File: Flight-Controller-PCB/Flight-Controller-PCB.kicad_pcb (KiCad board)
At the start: 2 copper layers, 50 x 50 mm, 77 parts, among them J1 ESC_1, J2 Receiver, J3 ESC_2, J4 ICSP, J5 ESC_3, J6 Aux, J7 ESC_4, J8 Power_In, J9 USB_B_Micro, Q1 BSS138, Q2 BSS138, Q3 PMV48XP,215, Q4 PMV48XP,215, SW1 Push-Switch, U1 MCP6001U, U2 ICM-20689, U3 ATmega32U4-AU, U4 LM1117-5.0, U5 LP2985-3.3, Y1 16MHz, CL 7pF

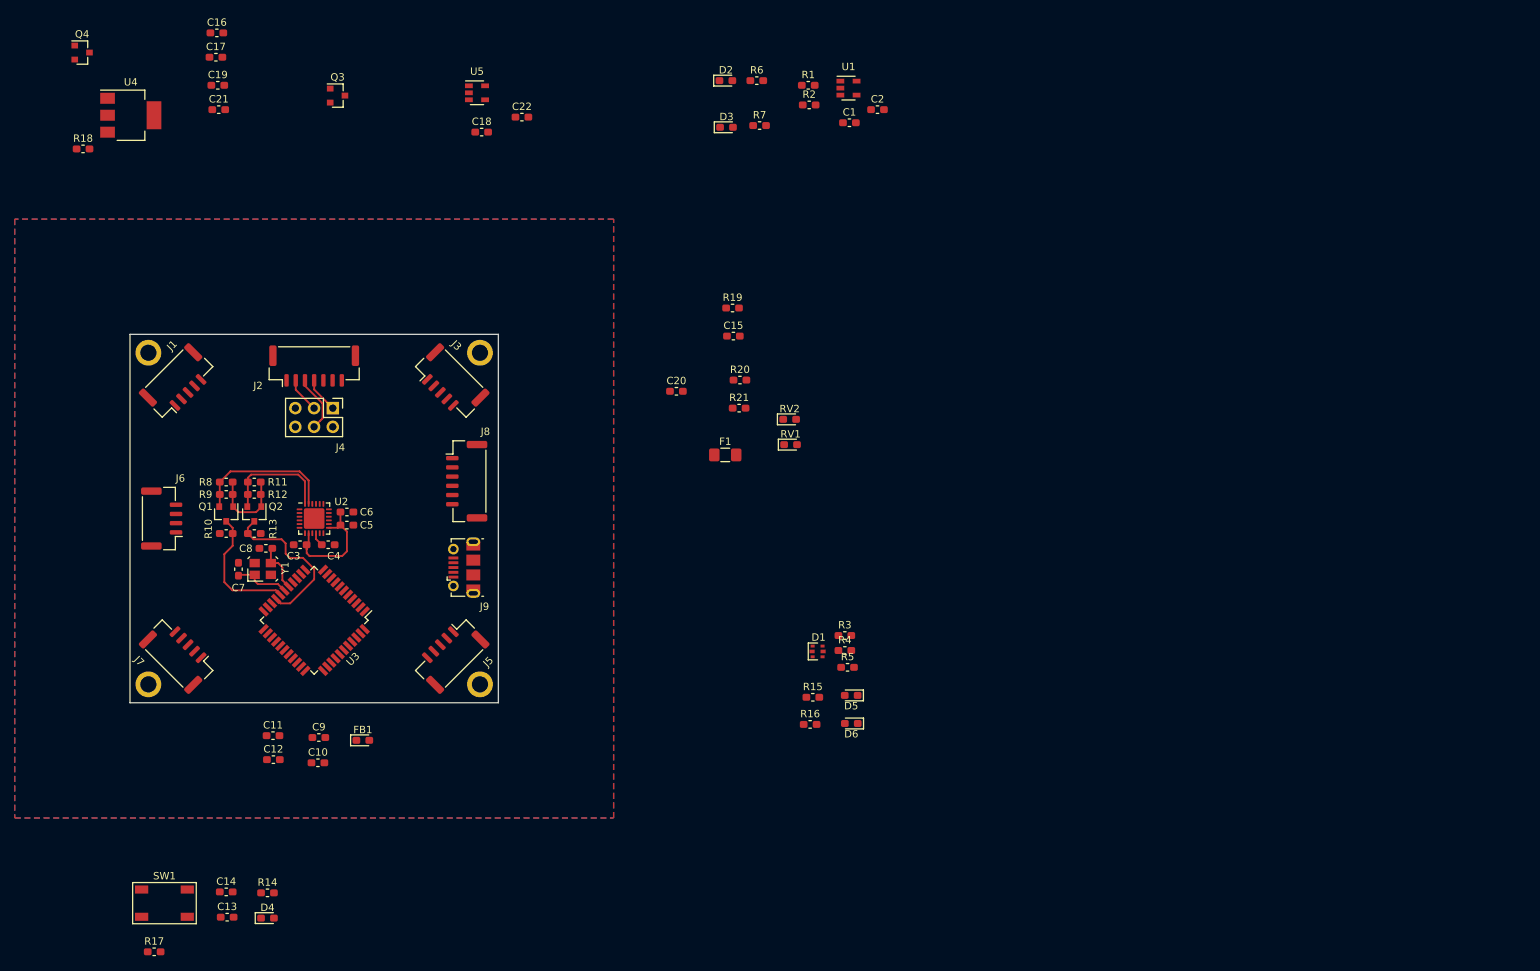
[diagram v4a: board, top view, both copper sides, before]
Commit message: Power regulators routed
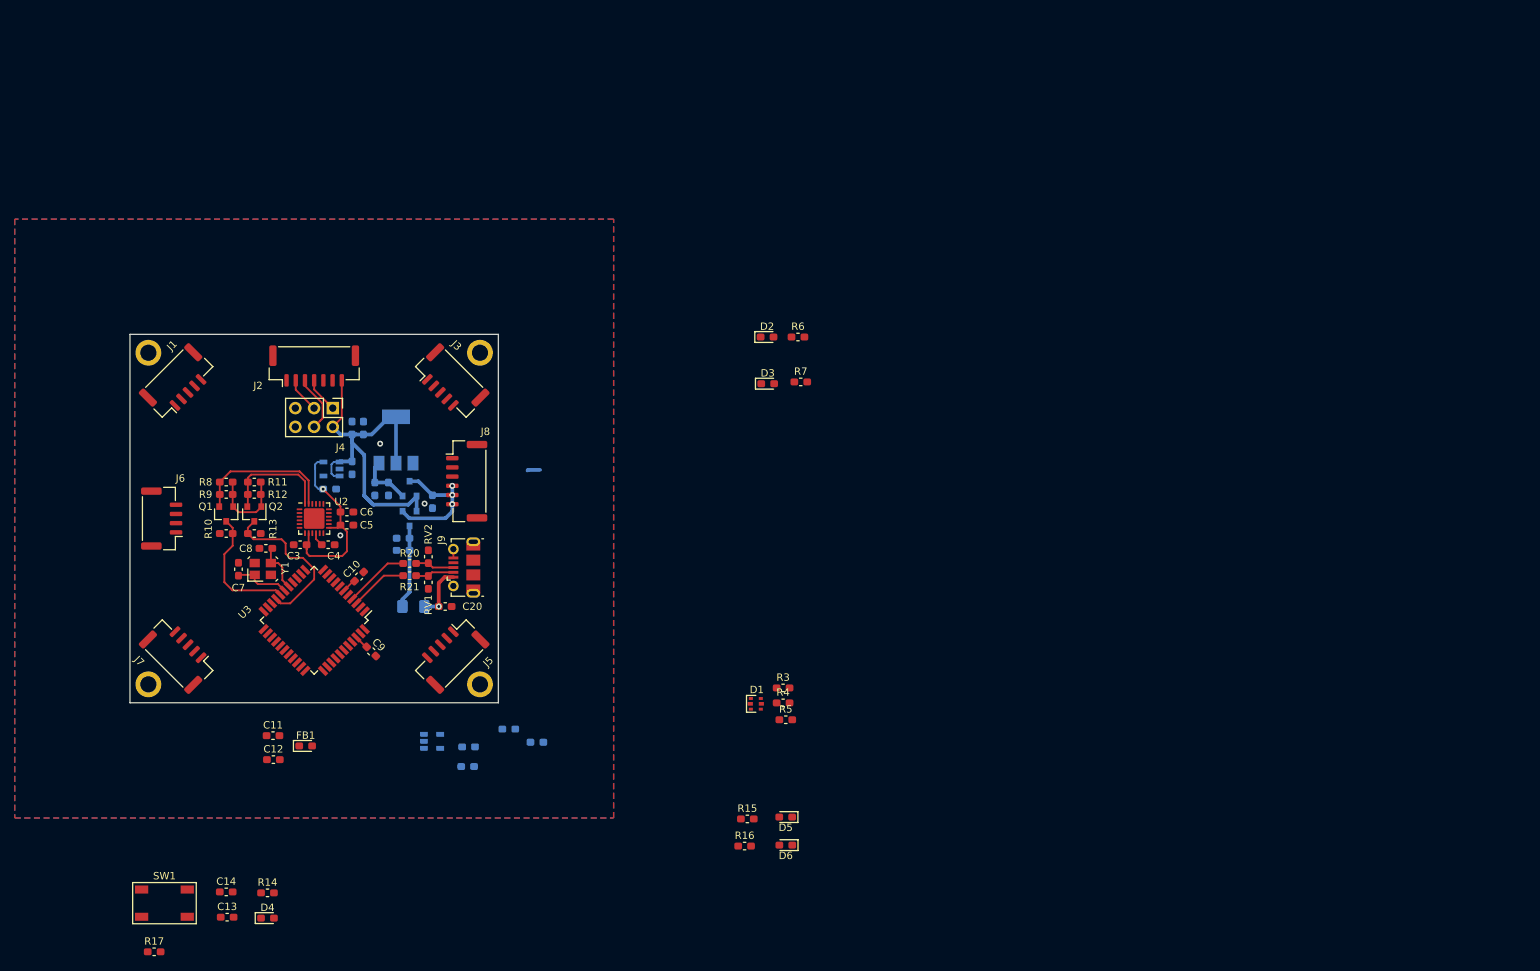
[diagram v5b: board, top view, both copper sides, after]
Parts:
- C1, C15, C16, C17, C18, C19, C2, C21, C22, F1, Q3, Q4, R1, R18, R19, R2, U1, U4, U5: moved to B.Cu
- RV1, RV2: footprint Diode_SMD:D_0603_1608Metric_Pad1.05x0.95mm_HandSolder -> Resistor_SMD:R_0603_1608Metric_Pad1.05x0.95mm_HandSolder
- moved U1 105.1 mm to (104.9, 144.5)
- moved R1 103.4 mm to (109.7, 148.0)
- moved R2 98.6 mm to (109.9, 145.3)
- moved C2 97.5 mm to (119.1, 144.7)
- moved C1 94.4 mm to (115.3, 142.9)
- moved Q4 74.0 mm to (101.9, 110.2), turned to 90 degrees
- moved R18 67.4 mm to (105.0, 112.0), turned to 90 degrees
- moved C16 66.1 mm to (99.0, 110.3), turned to 270 degrees
- moved C17 62.4 mm to (97.1, 110.3), turned to 270 degrees
- moved Q3 58.2 mm to (101.9, 114.3), turned to 270 degrees
- moved U4 56.9 mm to (100.0, 103.6), turned to 90 degrees
- moved C22 56.8 mm to (91.0, 110.3)
- moved R19 55.5 mm to (101.0, 118.6)
- moved U5 54.7 mm to (91.2, 107.6), turned to 180 degrees
- moved RV1 52.6 mm to (104.4, 123.0), turned to 270 degrees
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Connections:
- J9 pad 2: D- -> Net-(J9-Pad2)
- J9 pad 3: D+ -> Net-(J9-Pad3)
- R20 pad 1: D+ -> Net-(J9-Pad3)
- R21 pad 2: D- -> Net-(J9-Pad2)
- RV1 pad 1: D- -> Net-(J9-Pad2)
- RV2 pad 1: D+ -> Net-(J9-Pad3)
- Y1 pad -: GND -> (no net)
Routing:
- net +5V: track 0.00 -> 55.6 mm
- net VDD: track 0.00 -> 17.6 mm, vias 0 -> 3
- net VBUS: track 0.00 -> 11.4 mm
- net +3V3: track 27.4 -> 37.1 mm, vias 0 -> 1
- net D+: track 0.00 -> 8.91 mm
- net D-: track 0.00 -> 7.90 mm
- net Net-(C20-Pad1): track 0.00 -> 7.46 mm, vias 0 -> 1
- net Net-(C16-Pad1): track 0.00 -> 7.39 mm
- net Net-(J9-Pad3): track 0.00 -> 5.33 mm
- net Net-(J9-Pad2): track 0.00 -> 5.29 mm
- net Net-(C10-Pad1): track 0.00 -> 1.98 mm
- net Net-(C9-Pad1): track 0.00 -> 1.93 mm
- net GND: track 0.00 -> 1.20 mm, vias 0 -> 3

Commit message: everything placed
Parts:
- added C23: 0.1uF 16V X7R 10%, Capacitor_SMD:C_0603_1608Metric_Pad1.05x0.95mm_HandSolder, F.Cu at (97.8, 126.4)
- C1, C2, R1, R2, U1: moved to F.Cu
- C20: moved to B.Cu
- FB1: footprint Diode_SMD:D_0603_1608Metric_Pad1.05x0.95mm_HandSolder -> Resistor_SMD:R_0603_1608Metric_Pad1.05x0.95mm_HandSolder
- moved R5 94.0 mm to (65.3, 107.7), turned to 90 degrees
- moved D6 92.6 mm to (66.6, 125.2), turned to 0 degrees
- moved D5 92.5 mm to (66.6, 121.5), turned to 0 degrees
- moved R4 90.1 mm to (68.2, 107.7), turned to 90 degrees
- moved D1 87.9 mm to (68.2, 104.4), turned to 270 degrees
- moved R3 86.6 mm to (71.1, 107.7), turned to 90 degrees
- moved R15 84.6 mm to (70.1, 121.5), turned to 180 degrees
- moved R16 84.2 mm to (70.1, 125.2), turned to 180 degrees
- moved R7 69.3 mm to (86.2, 104.5), turned to 180 degrees
- moved SW1 66.7 mm to (78.7, 100.6)
- moved D3 65.1 mm to (86.2, 106.3), turned to 180 degrees
- moved D4 63.6 mm to (74.4, 105.4), turned to 270 degrees
- moved C13 63.3 mm to (83.1, 105.4), turned to 270 degrees
- moved R14 60.0 mm to (76.2, 105.4), turned to 90 degrees
- moved C14 59.7 mm to (81.3, 105.4), turned to 270 degrees
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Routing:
- net +5V: track 55.6 -> 83.0 mm
- net RESET: track 0.00 -> 22.5 mm
- net A0: track 0.00 -> 8.42 mm
- net D8: track 0.00 -> 7.69 mm
- net VDD: track 17.6 -> 25.2 mm
- net D9: track 0.00 -> 5.23 mm
- net Net-(R1-Pad1): track 0.00 -> 3.49 mm
- net /G_RGB: track 0.00 -> 2.92 mm
- net /B_RGB: track 0.00 -> 2.92 mm
- net Net-(R17-Pad1): track 0.00 -> 2.17 mm
- net Net-(D5-Pad2): track 0.00 -> 1.81 mm
- net Net-(D6-Pad2): track 0.00 -> 1.81 mm
- net Net-(D3-Pad2): track 0.00 -> 1.81 mm
- net /R_RGB: track 0.00 -> 1.68 mm
- net Net-(D2-Pad2): track 0.00 -> 1.65 mm

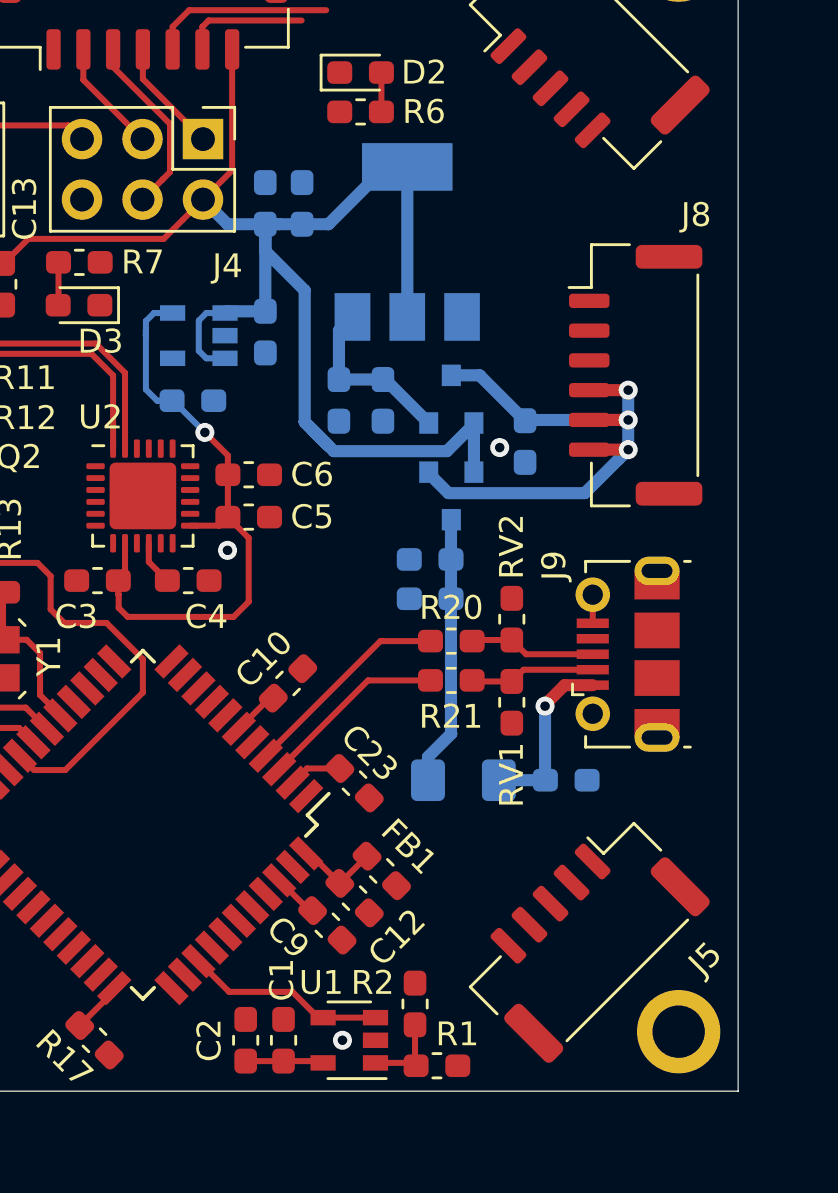
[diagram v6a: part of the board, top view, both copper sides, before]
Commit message: Moved all components to the top of the board
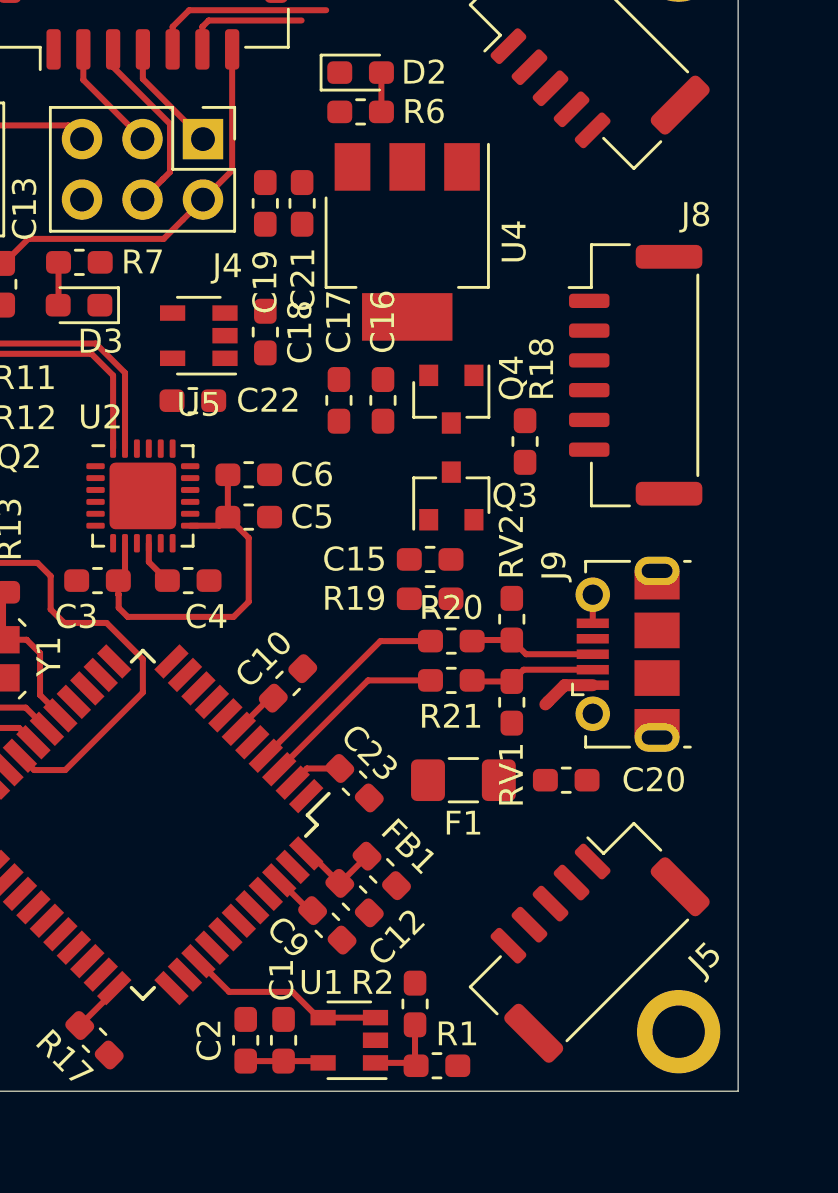
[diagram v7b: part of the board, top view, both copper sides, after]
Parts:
- C15, C16, C17, C18, C19, C20, C21, C22, F1, Q3, Q4, R18, R19, U4, U5: moved to F.Cu
- turned C16 to 90 degrees
- turned C17 to 90 degrees
- turned C18 to 90 degrees
- turned C19 to 270 degrees
- turned C21 to 270 degrees
- turned Q3 to 90 degrees
- turned Q4 to 270 degrees
- turned R18 to 270 degrees
- turned U4 to 270 degrees
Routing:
- net +5V: track 83.0 -> 35.9 mm
- net VDD: track 25.2 -> 0.00 mm, vias 3 -> 0
- net VBUS: track 11.4 -> 0.00 mm
- net +3V3: track 37.2 -> 27.4 mm, vias 1 -> 0
- net Net-(C16-Pad1): track 7.39 -> 0.00 mm
- net Net-(C20-Pad1): track 7.40 -> 2.32 mm, vias 1 -> 0
- net GND: vias 3 -> 0

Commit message: 35 some traces left
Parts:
- moved R18 3.30 mm to (105.0, 108.7)
- moved R17 1.98 mm to (85.6, 135.6), turned to 135 degrees
- moved D5 0.35 mm to (66.2, 121.5)
- moved D6 0.35 mm to (66.2, 125.2)
- moved R15 0.14 mm to (70.2, 121.5)
- moved R16 0.10 mm to (70.2, 125.2)
- turned Q3 to 270 degrees
- turned Q4 to 90 degrees
- turned U4 to 90 degrees
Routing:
- net +5V: track 35.9 -> 256.5 mm
- net VDD: track 0.00 -> 52.7 mm
- net VBUS: track 0.00 -> 24.4 mm
- net +3V3: track 27.4 -> 48.0 mm, vias 0 -> 2
- net Net-(C16-Pad1): track 0.00 -> 17.3 mm
- net D8: track 7.69 -> 0.00 mm
- net Net-(C20-Pad1): track 2.32 -> 7.61 mm
- net D9: track 5.23 -> 0.00 mm
- net GND: track 1.20 -> 4.86 mm, vias 0 -> 10
